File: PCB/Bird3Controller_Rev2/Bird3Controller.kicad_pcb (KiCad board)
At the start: 2 copper layers, 43 x 108 mm, 49 parts, among them IC2 LM3519MK-20_NOPB, IC3 LM3405AXMY_NOPB, J1 Bird 3 24-pin Connector, J2 TXW154028S0 Connector, J3 2171800001, SW1 SW_Boot, SW2 SW_Reset, U1 ESP32-S3-WROOM-1, U3 SN65HVD231, U4 PLMR36520ADDAR

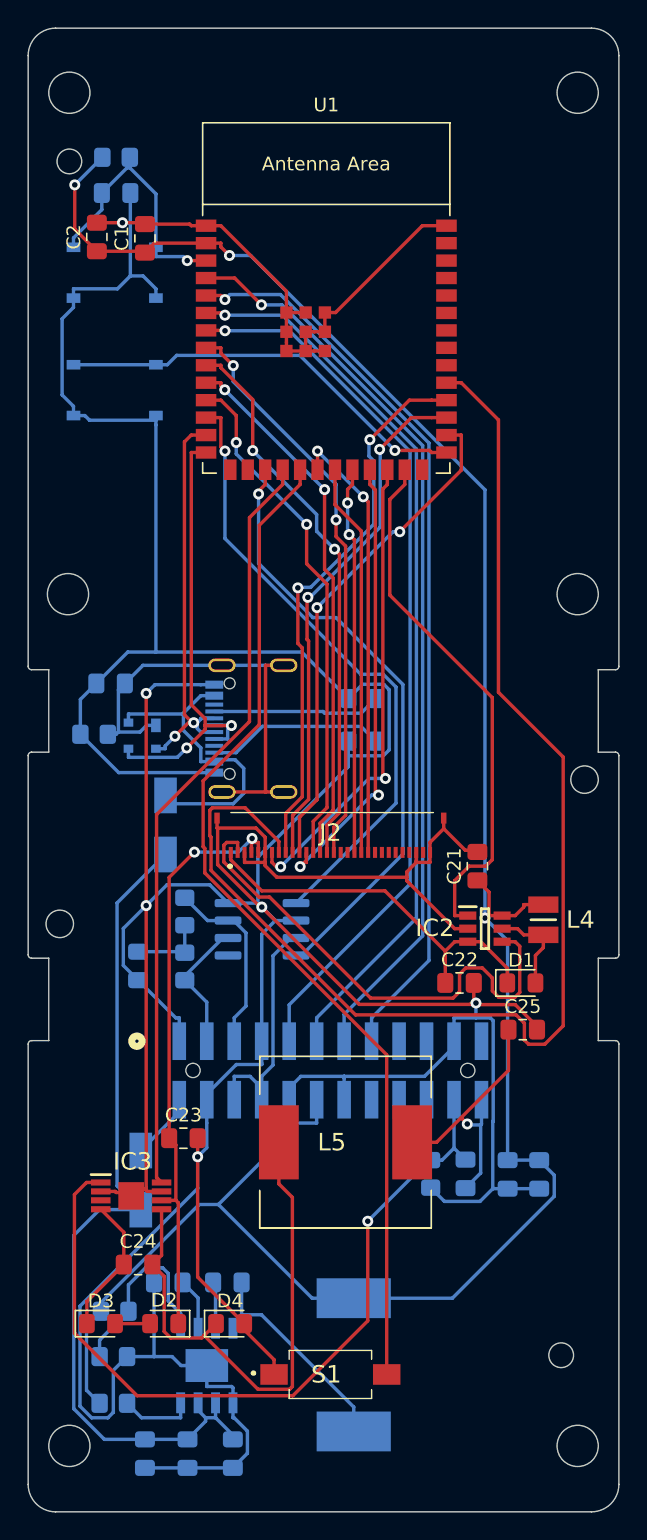
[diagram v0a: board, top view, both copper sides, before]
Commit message: Add 22-pin connector, new headlight circuit, etc. for Rev 2
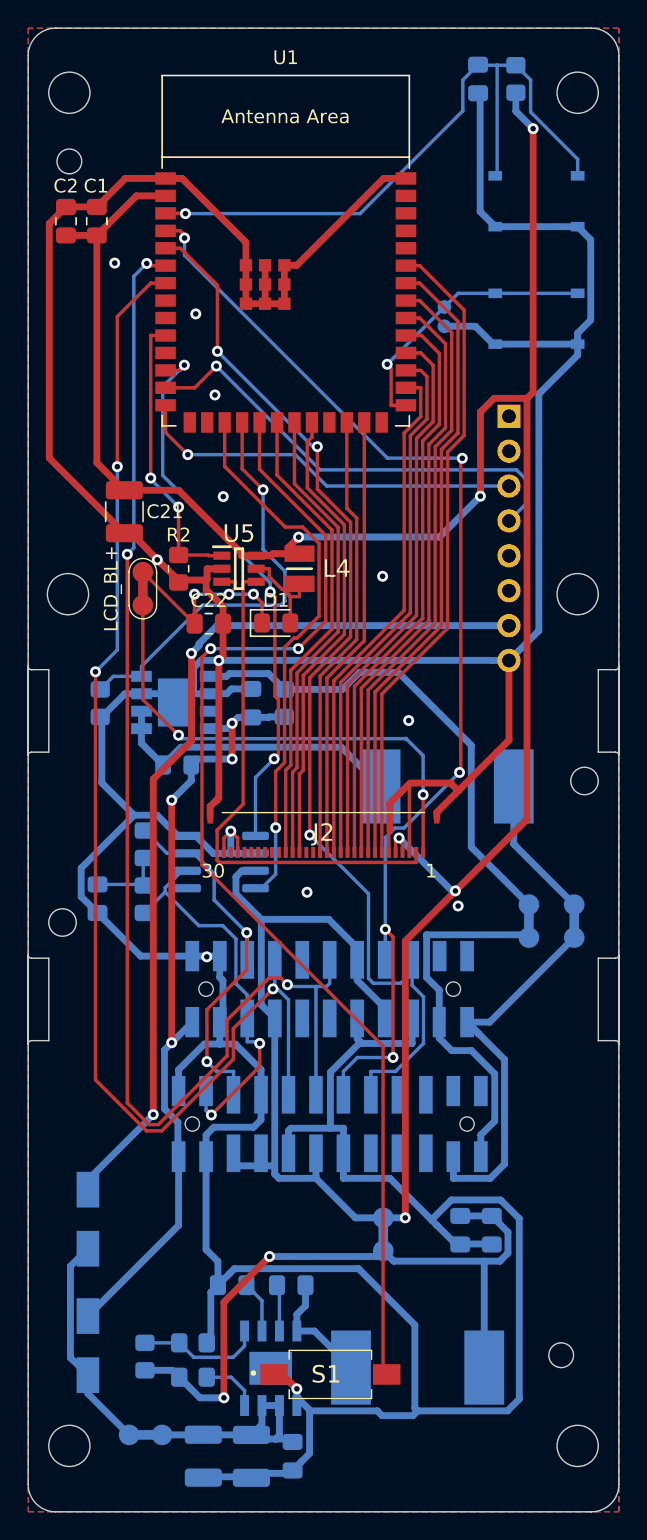
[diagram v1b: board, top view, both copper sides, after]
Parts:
- removed C23: 10u, Capacitor_SMD:C_0805_2012Metric_Pad1.18x1.45mm_HandSolder
- removed C24: 0.01u, Capacitor_SMD:C_0805_2012Metric_Pad1.18x1.45mm_HandSolder
- removed C25, C26: 1u, Capacitor_SMD:C_0805_2012Metric_Pad1.18x1.45mm_HandSolder
- removed C4: 4n7, Capacitor_SMD:C_0805_2012Metric_Pad1.18x1.45mm_HandSolder
- removed D2, D4: D_Schottky_Small, Diode_SMD:D_0805_2012Metric_Pad1.15x1.40mm_HandSolder
- removed D7: PRTR5V0U2X, Package_TO_SOT_SMD:SOT-143
- removed IC3: LM3405AXMY_NOPB, Bird3Controller:SOP65P490X109-9N
- removed L5: 27u, Bird3Controller:SRR1240270M
- removed R14: 0.953Ω, Resistor_SMD:R_0805_2012Metric_Pad1.20x1.40mm_HandSolder
- removed R4: 1M, Resistor_SMD:R_0805_2012Metric_Pad1.20x1.40mm_HandSolder
- added C8: 10u, Capacitor_SMD:C_0805_2012Metric_Pad1.18x1.45mm_HandSolder, B.Cu at (176.7, 91.1)
- added J4: ~, Bird3Controller:Adafruit USB-C Breakout, B.Cu at (195.5, 70.2)
- added L1: 100u, Bird3Controller:SRR1240270M, B.Cu at (191.0, 97.2)
- added R7: 0.200Ω, Resistor_SMD:R_0805_2012Metric_Pad1.20x1.40mm_HandSolder, B.Cu at (179.1, 91.1)
- added TP1: LCD_BL+, Bird3Controller:TestPointBridge_2Pads_D1.5mm, F.Cu at (168.8, 82.8)
- added TP2: 3V3, Bird3Controller:TestPointBridge_2Pads_D1.5mm, B.Cu at (186.3, 129.8)
- added TP3: VIN, Bird3Controller:TestPointBridge_2Pads_D1.5mm, B.Cu at (169.1, 144.4)
- added TP4: LED+, Bird3Controller:TestPointBridge_2Pads_D1.5mm, B.Cu at (196.9, 107.0)
- added TP5: LED-, Bird3Controller:TestPointBridge_2Pads_D1.5mm, B.Cu at (200.2, 107.0)
- added TP_Boot1: TestPoint_2Pole, Bird3Controller:TestPoint_2Pads_D1.0mm, B.Cu at (190.8, 63.0)
- added U2: ~, Bird3Controller:Diodes_SO-8EP, B.Cu at (171.2, 91.1)
- C14, C16, C21: footprint Capacitor_SMD:C_0805_2012Metric_Pad1.18x1.45mm_HandSolder -> Capacitor_SMD:C_1210_3225Metric_Pad1.33x2.70mm_HandSolder
- D3: moved to B.Cu
- J3: value 2171800001 -> 87832-2220; footprint Bird3Controller:MOLEX_2171800001 -> Bird3Controller:878322220
- L3: value SRR1260-100M -> 10u
- R2: value 5k1 -> 10k; moved to F.Cu
- R3: value 5k1 -> 10k
- U4: value PLMR36520ADDAR -> LMR36520ADDAR
- moved D3 41.0 mm to (171.3, 95.6), turned to 180 degrees
- moved C21 36.4 mm to (167.5, 77.2), turned to -90 degrees
- moved C22 31.9 mm to (173.7, 85.3)
- moved U5 31.7 mm to (175.8, 81.3)
- moved D1 31.7 mm to (178.6, 85.3)
- moved SW1 31.1 mm to (197.5, 63.1)
- moved SW2 31.1 mm to (197.5, 54.6)
- moved L4 31.1 mm to (180.2, 81.3)
- moved R1 29.7 mm to (196.0, 45.7), turned to -90 degrees
- moved D6 29.3 mm to (164.8, 128.7)
- moved C3 27.6 mm to (193.2, 45.7), turned to 90 degrees
- moved R3 19.1 mm to (165.7, 91.1), turned to 90 degrees
- moved J3 19.0 mm to (182.4, 112.0), turned to 0 degrees
- moved R2 18.3 mm to (171.4, 81.3), turned to 90 degrees
- moved D5 12.7 mm to (164.8, 137.9)
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- renumbered IC2 to U5
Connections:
- C14 pad 1: Net-(D5-K) -> Net-(U4-EN)
- C15 pad 1: Net-(D5-K) -> Net-(U4-EN)
- C16 pad 1: Net-(D5-K) -> Net-(U4-EN)
- C18 pad 1: +3V3 -> Net-(C18-Pad1)
- C20 pad 1: +3V3 -> Net-(C18-Pad1)
- C22 pad 1: /LCD_BL+ -> Net-(D1-K)
- D1 pad 1: /LCD_BL+ -> Net-(D1-K)
- D3 pad 1: Net-(D3-K) -> +36V
- J1 pad 21: GND -> unconnected-(J1-SPK--Pad21)
- J1 pad 23: /SPK+ -> unconnected-(J1-SPK+-Pad23)
- J2 pad 4: +3.3V -> +3V3
- J2 pad 5: +3.3V -> +3V3
- L3 pad 2: +3V3 -> Net-(C18-Pad1)
- R11 pad 2: +3V3 -> Net-(C18-Pad1)
- R12 pad 2: +3V3 -> Net-(C18-Pad1)
- R2 pad 1: Net-(J3-CC2) -> GND
- R2 pad 2: GND -> /LCD_BL_SIG
- R3 pad 1: Net-(J3-CC1) -> GND
- R3 pad 2: GND -> /LED_SIG
- U1 pad 10: /LCD_DB0 -> /LCD_BL_SIG
- U1 pad 11: /LCD_DB1 -> unconnected-(U1-GPIO18-Pad11)
- U1 pad 23: /LCD_DB2 -> unconnected-(U1-GPIO21-Pad23)
- U1 pad 24: /LCD_DB7 -> /LCD_WR
- U1 pad 25: /LCD_BL_SIG -> /LCD_RD
- U1 pad 28: /LCD_DB3 -> /LCD_DB0
- U1 pad 29: /LCD_DB4 -> /LCD_DB1
- U1 pad 30: /LCD_DB5 -> /LCD_DB2
- U1 pad 31: /LCD_DB6 -> /LCD_DB3
- U1 pad 32: unconnected-(U1-GPIO39-Pad32) -> /LCD_DB4
- U1 pad 33: unconnected-(U1-GPIO40-Pad33) -> /LCD_DB5
- U1 pad 34: unconnected-(U1-GPIO41-Pad34) -> /LCD_DB6
- U1 pad 35: unconnected-(U1-GPIO42-Pad35) -> /LCD_DB7
- U1 pad 8: /LCD_WR -> unconnected-(U1-GPIO15-Pad8)
- U1 pad 9: /LCD_RD -> unconnected-(U1-GPIO16-Pad9)
- U4 pad 2: Net-(D5-K) -> Net-(U4-EN)
- U4 pad 3: Net-(D5-K) -> Net-(U4-EN)
- U5 pad 3: /LCD_BL+ -> Net-(D1-K)
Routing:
- net +36V: track 4.86 -> 59.7 mm, vias 0 -> 4
- net Net-(C18-Pad1): track 0.00 -> 49.6 mm, vias 0 -> 2
- net /LCD_DB6: track 94.4 -> 46.1 mm
- net Net-(D5-K): track 62.8 -> 15.8 mm
- net +3.3V: track 43.3 -> 0.00 mm, vias 2 -> 0
- net +5V: track 23.0 -> 66.2 mm, vias 0 -> 2
- net Net-(D4-K): track 40.2 -> 0.00 mm
- net Net-(U2-SET): track 0.00 -> 35.6 mm
- net Net-(D7-GND): track 34.7 -> 0.00 mm
- net +3V3: track 188.8 -> 219.2 mm, vias 3 -> 6
- net Net-(U1-EN): track 19.4 -> 49.3 mm
- net /LED-: track 58.3 -> 28.8 mm, vias 1 -> 0
- net /BR1: track 65.5 -> 94.4 mm, vias 1 -> 3
- net /BR2: track 65.1 -> 91.2 mm, vias 1 -> 3
- net /LED_SIG: track 55.8 -> 30.8 mm, vias 0 -> 1
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- added copper zone on B.Cu, net GND
- added copper zone on F.Cu, net GND
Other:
- outline, holes or cut-outs redrawn
- board text added: "locked"

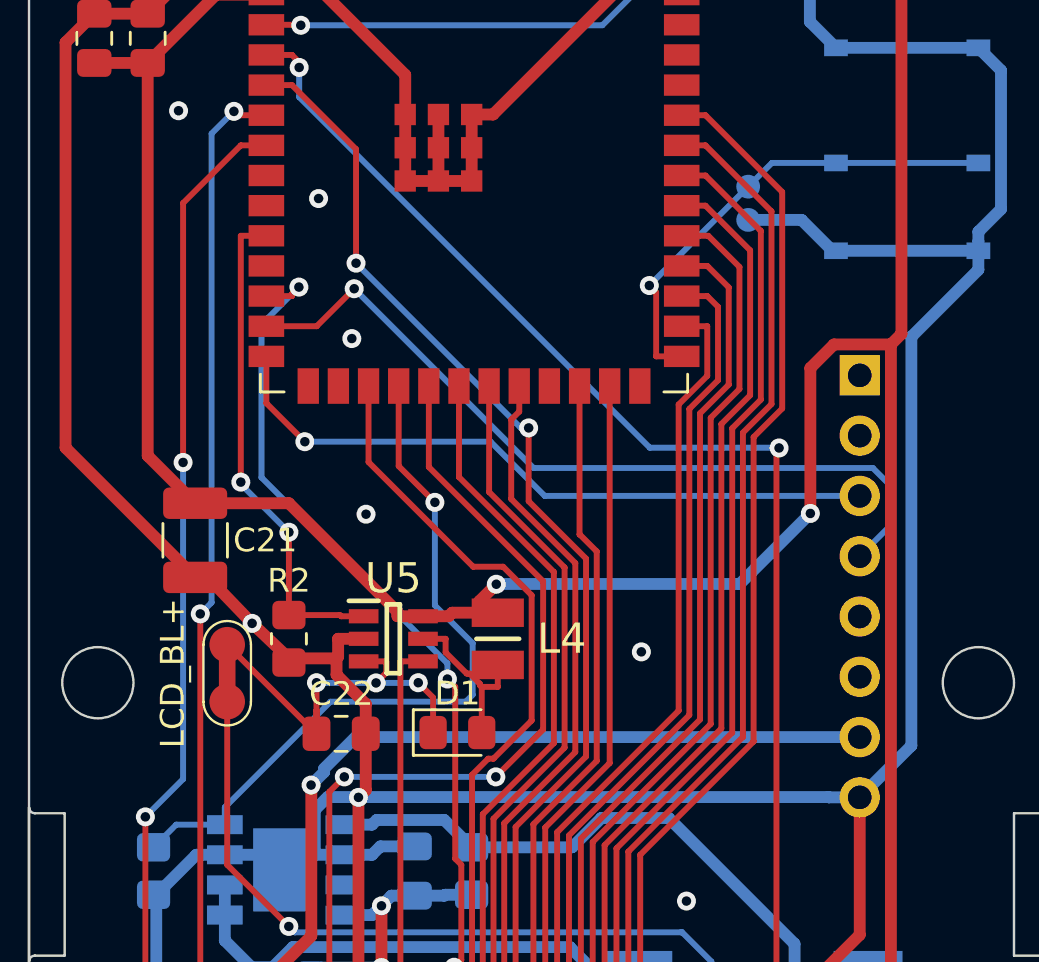
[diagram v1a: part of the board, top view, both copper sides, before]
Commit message: Add circuit to selectively ground the `PWR_ENA` pin
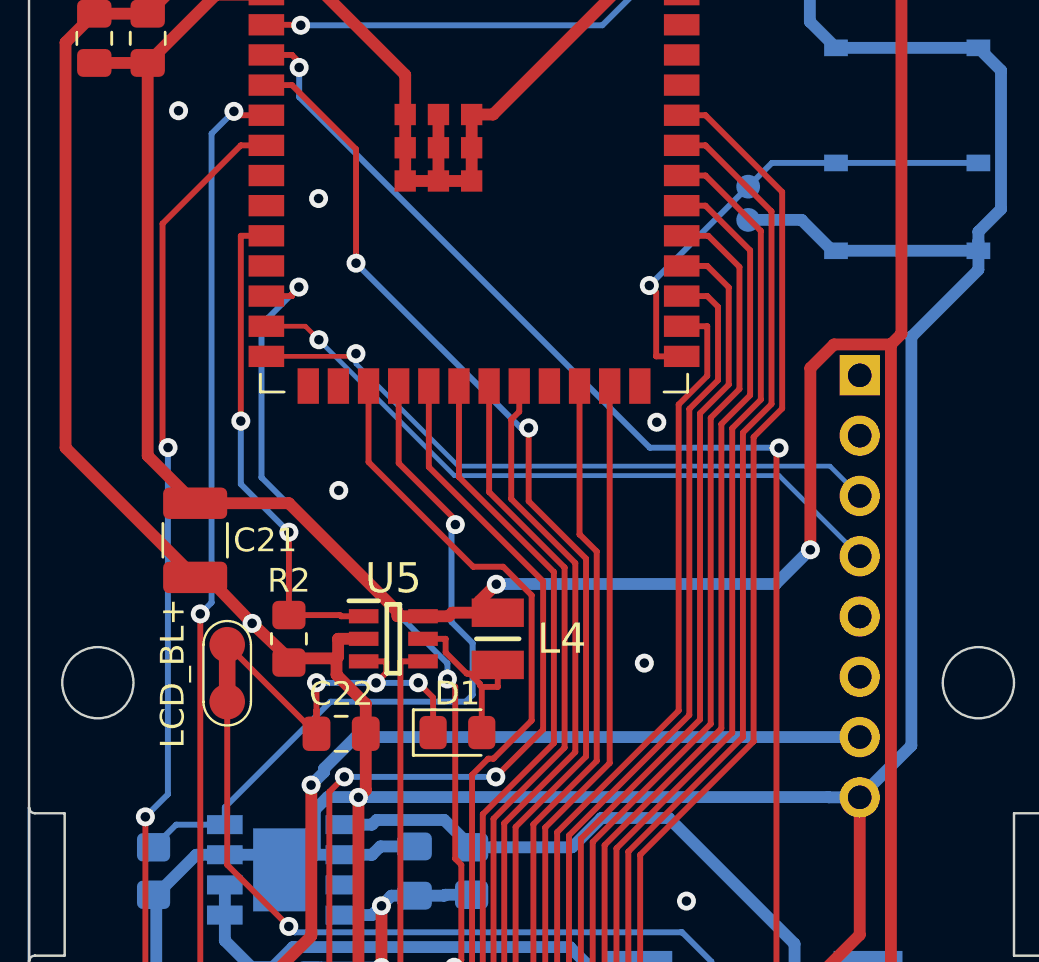
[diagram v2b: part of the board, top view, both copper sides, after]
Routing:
- net /USB_D-: track 33.8 -> 29.0 mm
- net +3V3: track 219.2 -> 220.1 mm
- net /USB_D+: track 28.6 -> 27.8 mm

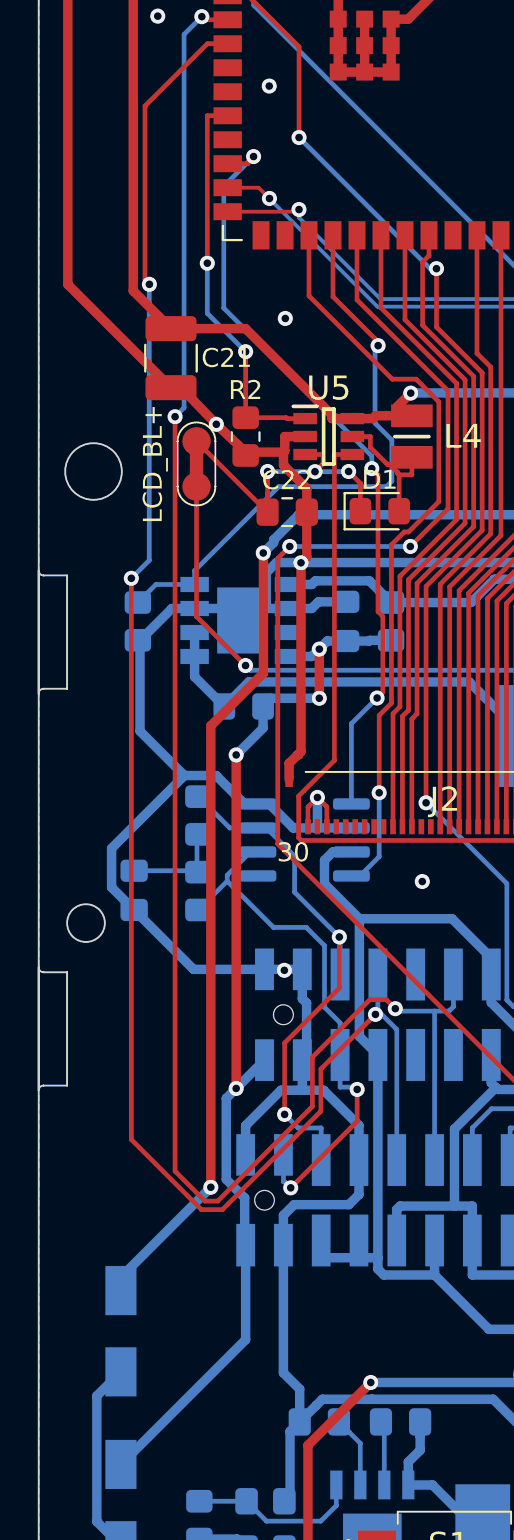
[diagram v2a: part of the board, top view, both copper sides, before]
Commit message: Add `PWR_ENA` mosfet and fuse to PCB
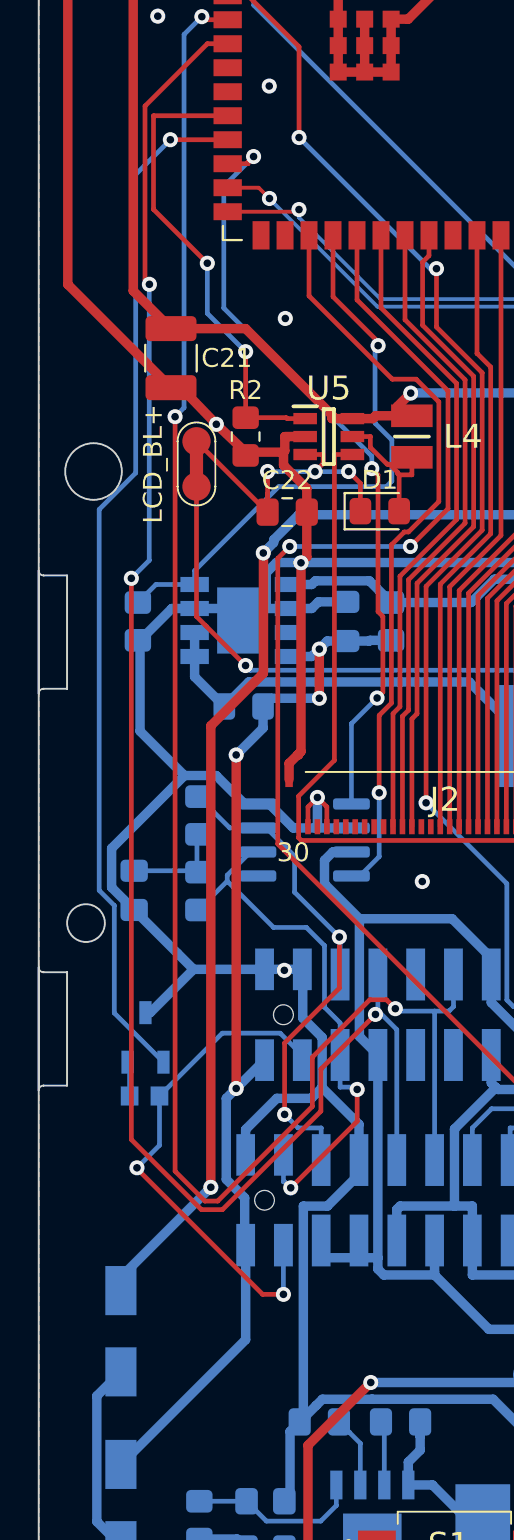
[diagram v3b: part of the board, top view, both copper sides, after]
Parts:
- added F1: Polyfuse_Small, Bird3Controller:FUSC1607X85N, B.Cu at (166.1, 116.2)
- added Q1: 2N7002A, Package_TO_SOT_SMD:TSOT-23, B.Cu at (166.2, 113.2)
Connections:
- J1 pad 4: GND -> /PWR_ENA
- J3 pad 4: GND -> /PWR_ENA
- U1 pad 11: unconnected-(U1-GPIO18-Pad11) -> /PWR_ENA_SIG
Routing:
- net /PWR_ENA_SIG: track 0.00 -> 54.8 mm, vias 0 -> 1
- net /PWR_ENA: track 0.00 -> 27.2 mm, vias 0 -> 2
- net /LCD_BL_SIG: track 21.1 -> 25.1 mm
- net Net-(Q1-S): track 0.00 -> 1.84 mm
- net GND: track 420.3 -> 421.8 mm
